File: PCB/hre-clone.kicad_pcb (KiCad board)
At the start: 2 copper layers, 155.5 x 76.9 mm, 23 parts, among them SW1 SW_DIP_x04, U1 74LS258, U10 MC6845, U11 MC6845, U12 DIL14, U13 7402, U2 74LS174, U3 74LS257, U4 74LS244, U5 2716, U6 2716, U7 74LS05, U8 74LS155, U9 74LS257

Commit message: Re-organize file, remove backup files, update readme
A little more organization always helps!
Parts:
- U1, U2, U3, U8, U9: footprint Housings_DIP:DIP-16_W7.62mm_LongPads -> Package_DIP:DIP-16_W7.62mm
- U12, U13, U7: footprint Housings_DIP:DIP-14_W7.62mm_LongPads -> Package_DIP:DIP-14_W7.62mm
- U4: footprint Housings_DIP:DIP-20_W7.62mm_LongPads -> Package_DIP:DIP-20_W7.62mm
- U5, U6: footprint Housings_DIP:DIP-24_W15.24mm_LongPads -> Package_DIP:DIP-24_W15.24mm

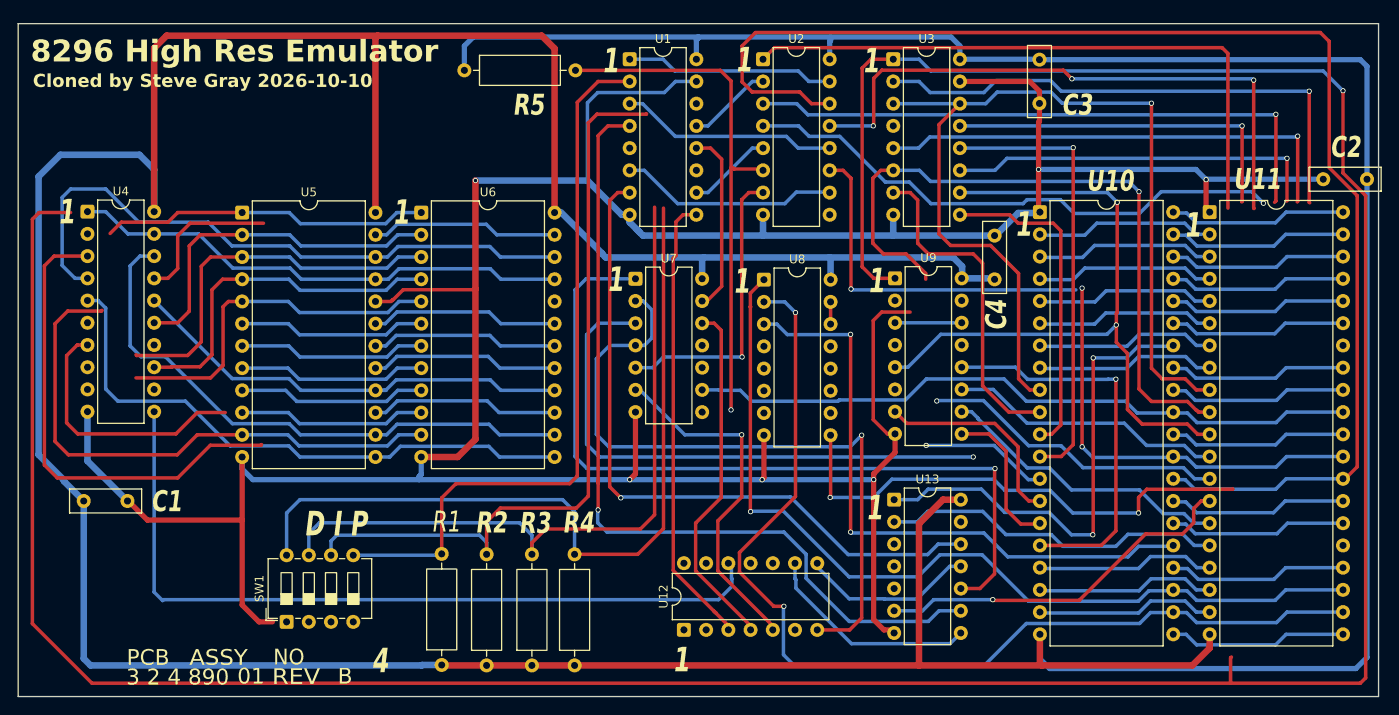
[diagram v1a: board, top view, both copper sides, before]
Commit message: Some additional PCB fixes
Getting closer to complete routing. Still some traces under chips that can not be determined.
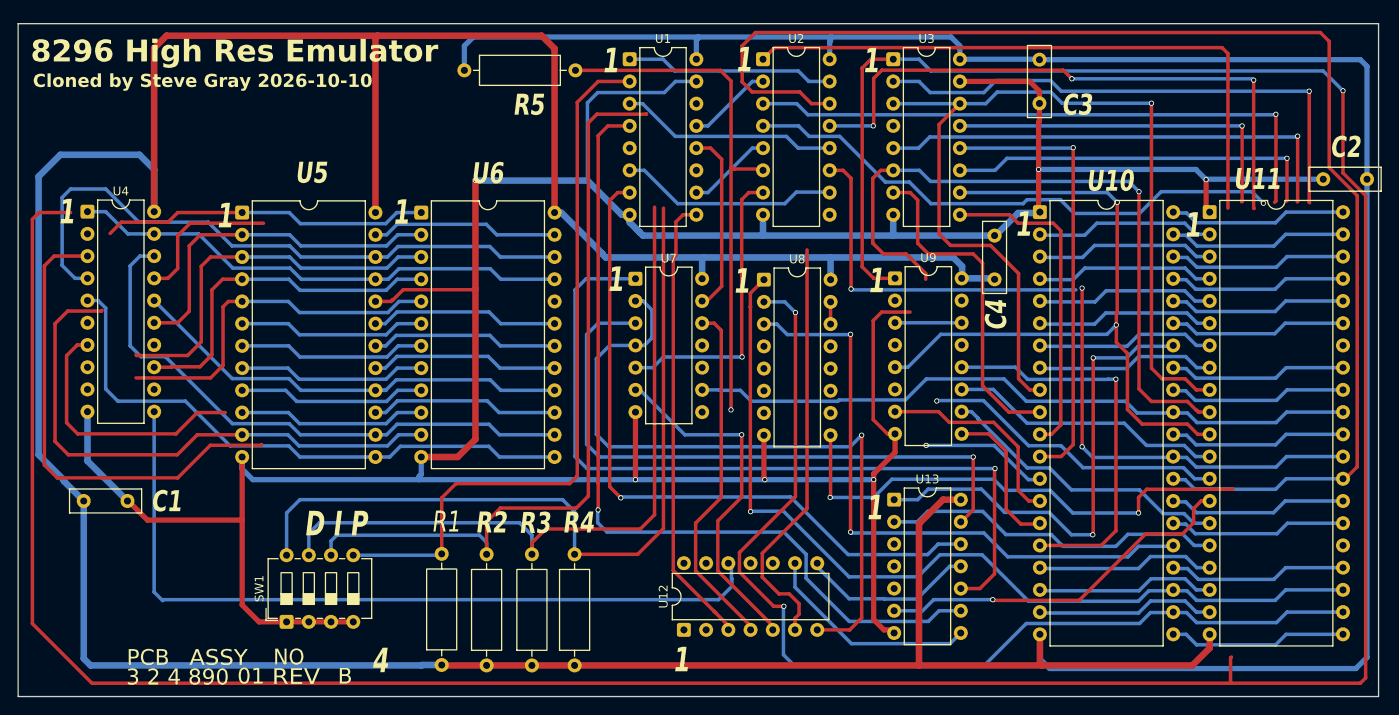
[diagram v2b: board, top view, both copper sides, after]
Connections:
- SW1 pad 1: unconnected-(SW1-Pad1) -> GND
- SW1 pad 2: unconnected-(SW1-Pad2) -> GND
- SW1 pad 3: unconnected-(SW1-Pad3) -> GND
- SW1 pad 4: unconnected-(SW1-Pad4) -> GND
- U13 pad 13: U13-13 -> U7-3
- U6 pad 20: GND -> unconnected-(U6-G-Pad20)
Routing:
- net unconnected-(U12-Pad6): track 0.00 -> 48.2 mm
- net GND: track 386.9 -> 395.8 mm, vias 6 -> 7
- net U7-3: track 63.4 -> 71.5 mm

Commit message: Updated schematics and routing
There are now zero unrouted connections, but a few remaining connections missing under the chips. Added a picture of the traces under the CRTC chip.
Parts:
- moved C2 0.50 mm to (246.7, 97.8)
- moved U8 0.10 mm to (178.2, 109.6)
- moved U9 0.05 mm to (193.1, 109.6)
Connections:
- U1 pad 11: unconnected-(U1-I0d-Pad11) -> DIP1
- U1 pad 14: unconnected-(U1-I0c-Pad14) -> DIP3
- U1 pad 5: unconnected-(U1-I0b-Pad5) -> DIP2
- U10 pad 13: MA9 -> MUX2A
- U10 pad 24: RS -> A0
- U11 pad 24: RS -> A0
- U11 pad 25: ~{CS} -> ~{CRTC_CS}
- U11 pad 34: RA4 -> unconnected-(U11-RA4-Pad34)
- U12 pad 6: unconnected-(U12-Pad6) -> U8-13
- U13 pad 3: U13-3 -> Net-(U13-Pad3)
- U13 pad 4: U13-4 -> Net-(U13-Pad3)
- U13 pad 5: U13-5 -> MA10
- U2 pad 1: U2-MR -> unconnected-(U2-~{Mr}-Pad1)
- U2 pad 11: D3 -> D4
- U2 pad 13: D4 -> D5
- U2 pad 14: D5 -> A0
- U2 pad 9: U2-CP -> LATCH
- U3 pad 11: U3-11 -> RA2
- U3 pad 13: U3-13 -> MA8
- U3 pad 2: U3-2 -> RA0
- U3 pad 5: U3-5 -> RA1
- U4 pad 1: U4-OE -> U3-SEL
- U4 pad 12: U4-12 -> Q0
- U4 pad 14: U4-14 -> Q2
- U4 pad 19: U4-OE -> U3-SEL
- U4 pad 2: U4-2 -> XA7
- U4 pad 3: U4-3 -> Q5
- U4 pad 7: U4-7 -> Q1
- U4 pad 8: U4-8 -> XA5
- U4 pad 9: U4-9 -> XA3
- U5 pad 21: U4-OE -> U3-SEL
- U6 pad 21: U4-OE -> U3-SEL
- U7 pad 8: U7-8 -> R5
- U8 pad 13: unconnected-(U8-A0-Pad13) -> U8-13
- U8 pad 14: Net-(U8-Eb1) -> GND
- U8 pad 15: Net-(U8-Eb1) -> GND
- U8 pad 4: unconnected-(U8-Q3a-Pad4) -> LATCH
- U8 pad 9: U8-9 -> ~{CRTC_CS}
- U9 pad 15: unconnected-(U9-OE-Pad15) -> GND
- U9 pad 2: unconnected-(U9-I0a-Pad2) -> MA6
- U9 pad 6: unconnected-(U9-I1b-Pad6) -> MA9
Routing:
- net A0: track 0.00 -> 166.4 mm
- net MA8: track 31.5 -> 105.2 mm, vias 0 -> 1
- net ~{CRTC_CS}: track 0.00 -> 73.0 mm, vias 0 -> 2
- net unconnected-(U2-~{Mr}-Pad1): track 0.00 -> 71.6 mm
- net U2-MR: track 71.6 -> 0.00 mm
- net RA0: track 20.4 -> 91.6 mm, vias 0 -> 1
- net Q5: track 21.6 -> 91.3 mm
- net RA1: track 20.4 -> 87.5 mm, vias 0 -> 1
- net U3-2: track 61.9 -> 0.00 mm, vias 1 -> 0
- net RA2: track 20.4 -> 79.8 mm, vias 0 -> 1
- net U3-SEL: track 361.5 -> 420.9 mm
- net U8-9: track 57.8 -> 0.00 mm, vias 2 -> 0
- net U4-OE: track 57.6 -> 0.00 mm
- net U4-3: track 55.2 -> 0.00 mm
- net U3-5: track 54.3 -> 0.00 mm, vias 1 -> 0
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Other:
- board size 155.5 x 76.9 mm -> 155.7 x 76.9 mm
- board text added: "Cloned by Steve Gray 2026-10-11"
- board text removed: "Cloned by Steve Gray 2026-10-10"

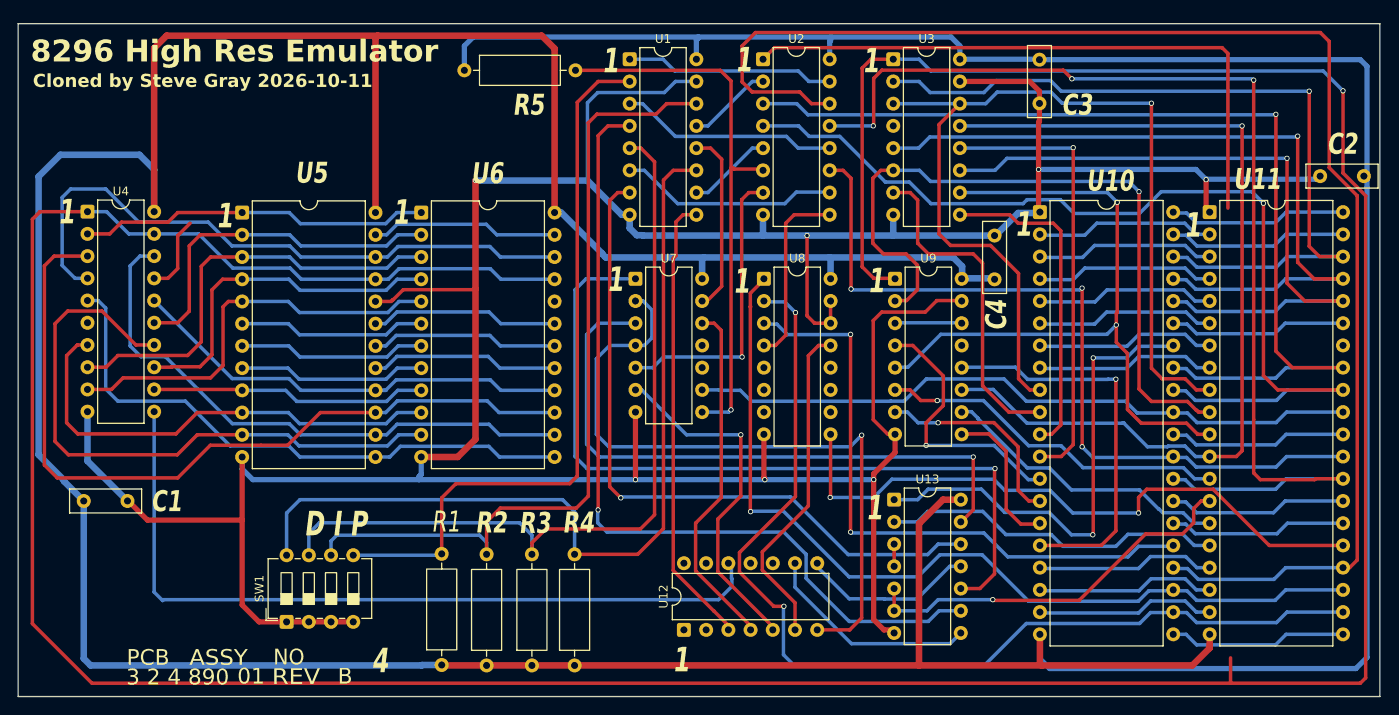
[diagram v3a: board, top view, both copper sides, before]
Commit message: Routing complete
Thanks to Andy Grady for corrections for some traces. DRC check ok. Updated many global labels, moved around some symbols, updated board text etc
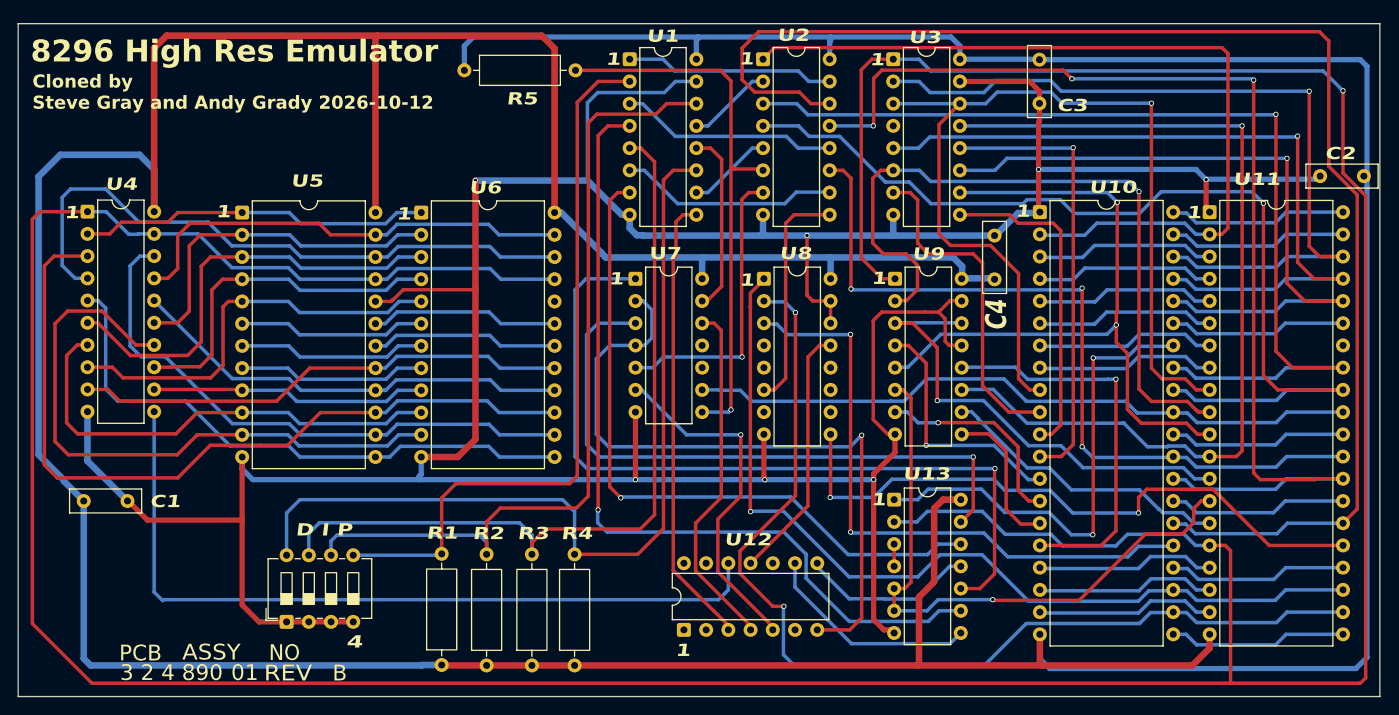
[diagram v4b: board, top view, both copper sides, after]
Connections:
- net EPROM_E renamed XA11
- net MUX3C renamed Net-(U1-Zc)
- net R5 renamed Net-(U2-D2)
- net U1-10 renamed LATCH1
- net U1-3 renamed LATCH4
- net U1-6 renamed LATCH3
- net U1-SEL renamed MUX1SEL
- net U13-11 renamed RIBBON-8
- net U13-8 renamed RIBBON-9
- net U2-2 renamed LATCH0
- net U4-11 renamed RIBBON-12
- net U7-1 renamed Net-(U13-Pad10)
- net U7-12 renamed ~{MUX3C}
- net U7-3 renamed Net-(U13-Pad13)
- net U7-4 renamed RIBBON-7
- net U7-5 renamed Net-(U2-Q2)
- net U7-6 renamed ~{LATCH2}
- U10 pad 24: A0 -> RS
- U11 pad 16: MA12 -> MUX2SEL
- U11 pad 24: A0 -> RS
- U12 pad 11: unconnected-(U12-Pad11) -> RIBBON-11
- U12 pad 6: U8-13 -> unconnected-(U12-Pad6)
- U13 pad 2: MA12 -> MUX2SEL
- U2 pad 1: unconnected-(U2-~{Mr}-Pad1) -> ~{RESET}
- U2 pad 14: A0 -> D7
- U3 pad 1: U3-SEL -> MUX2SEL
- U4 pad 1: U3-SEL -> MUX2SEL
- U4 pad 17: U4-17 -> XA8
- U4 pad 19: U3-SEL -> MUX2SEL
- U4 pad 6: U4-6 -> XA5
- U4 pad 8: XA5 -> XA3
- U4 pad 9: XA3 -> Q7
- U5 pad 21: U3-SEL -> MUX2SEL
- U6 pad 21: U3-SEL -> MUX2SEL
- U7 pad 10: U7-10 -> unconnected-(U7-Pad10)
- U8 pad 13: U8-13 -> RIBBON-11
- U8 pad 4: LATCH -> unconnected-(U8-Q3a-Pad4)
- U8 pad 6: unconnected-(U8-Q1a-Pad6) -> LATCH
- U9 pad 1: U3-SEL -> MUX2SEL
- U9 pad 13: unconnected-(U9-I1c-Pad13) -> GND
- U9 pad 14: Net-(U9-I0c) -> MA9
- U9 pad 3: Net-(U9-I0c) -> MA9
- U9 pad 6: MA9 -> MA10
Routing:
- net MUX2SEL: track 0.00 -> 474.6 mm, vias 0 -> 1
- net U3-SEL: track 420.9 -> 0.00 mm, vias 1 -> 0
- net A0: track 166.4 -> 0.00 mm
- net D7: track 20.4 -> 160.5 mm
- net ~{RESET}: track 20.5 -> 96.8 mm
- net unconnected-(U2-~{Mr}-Pad1): track 71.6 -> 0.00 mm
- net MA12: track 39.3 -> 0.00 mm
- net U8-13: track 38.1 -> 0.00 mm
- net Q7: track 21.6 -> 56.6 mm
- net XA8: track 21.5 -> 52.1 mm
- net RIBBON-11: track 0.00 -> 29.4 mm
- net MA10: track 44.8 -> 70.3 mm
- net RS: track 0.00 -> 20.5 mm
- net MA9: track 40.2 -> 54.6 mm
- net U4-17: track 8.93 -> 0.00 mm
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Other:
- board text added: "Cloned by Steve Gray and Andy Grady 2026-10-12"
- board text removed: "Cloned by Steve Gray 2026-10-11"
